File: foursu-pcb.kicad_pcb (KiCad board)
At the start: 2 copper layers, 71.4 x 38.1 mm, 24 parts, among them SW1 SW_Push, U1 ATmega32U4-AU, Y1 16MHz

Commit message: uh yes microcontroller stuff
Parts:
- moved C3 13.9 mm to (37.3, 129.1), turned to 270 degrees
- moved C2 8.76 mm to (46.8, 129.4), turned to 90 degrees
- moved C4 8.72 mm to (32.4, 136.5)
- moved C6 8.33 mm to (34.3, 133.3)
- moved Y1 6.54 mm to (42.1, 129.1), turned to 180 degrees
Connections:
- C2 pad 2: Net-(C2-Pad2) -> GND
- C3 pad 2: Net-(C2-Pad2) -> GND
- U1 pad 27: Net-(U1-Pad27) -> ROW0
- U1 pad 28: Net-(U1-Pad28) -> ROW1
- U1 pad 29: Net-(U1-Pad29) -> COL0
- U1 pad 30: Net-(U1-Pad30) -> COL1
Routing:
- net GND: track 0.00 -> 110.4 mm
- net +5V: track 0.00 -> 91.0 mm, vias 0 -> 5
- net ROW1: track 0.00 -> 58.3 mm
- net COL1: track 0.00 -> 57.5 mm, vias 0 -> 1
- net ROW0: track 0.00 -> 54.5 mm
- net COL0: track 0.00 -> 32.4 mm, vias 0 -> 1
- net Net-(R3-Pad2): track 0.00 -> 29.2 mm, vias 0 -> 2
- net Net-(C3-Pad1): track 0.00 -> 12.7 mm
- net Net-(C2-Pad1): track 3.70 -> 10.6 mm
- net Net-(D2-Pad2): track 0.00 -> 6.82 mm
- net Net-(D4-Pad2): track 0.00 -> 6.62 mm
- net Net-(D1-Pad2): track 0.00 -> 6.62 mm
- net Net-(D3-Pad2): track 0.00 -> 6.62 mm
- net Net-(C4-Pad1): track 0.00 -> 6.32 mm
- net VCC: track 0.00 -> 5.07 mm
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
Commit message: finished first prototype?
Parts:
- removed C1, C5, C6: 0.1uF, Capacitor_SMD:C_0805_2012Metric
- removed C2, C3: 22pF, Capacitor_SMD:C_0805_2012Metric
- removed C4: 1uF, Capacitor_SMD:C_0805_2012Metric
- removed C7: 10uF, Capacitor_SMD:C_0805_2012Metric
- removed F1: Polyfuse, Fuse:Fuse_1206_3216Metric
- removed R1, R2: 22, Resistor_SMD:R_0805_2012Metric
- removed R3, R4: 10k, Resistor_SMD:R_0805_2012Metric
- removed U1: ATmega32U4-AU, Package_QFP:TQFP-44_10x10mm_P0.8mm
- removed USB1: Molex-0548190519, random-keyboard-parts:Molex-0548190589
- removed Y1: 16MHz, Crystal:Crystal_SMD_3225-4Pin_3.2x2.5mm
- added B1: SPARKFUN_PRO_MICRO, Boards:SPARKFUN_PRO_MICRO, F.Cu at (57.5, 137.5)
- added D5: 1N4148, Diode_THT:D_DO-35_SOD27_P7.62mm_Horizontal, B.Cu at (91.6, 161.8)
- D1, D2, D3, D4: value SOD-123 -> 1N4148; footprint Diode_SMD:D_SOD-123 -> Diode_THT:D_DO-35_SOD27_P7.62mm_Horizontal
- MX1, MX2, MX3, MX4: value MX-NoLED -> MX-LED; footprint MX_Alps_Hybrid:MX-1U-NoLED -> MX_Only:MXOnly-1U
- SW1: value SW_Push -> Rotary_Encoder_Switch; footprint random-keyboard-parts:SKQG-1155865 -> Rotary_Encoder:RotaryEncoder_Alps_EC11E-Switch_Vertical_H20mm; moved to F.Cu
- moved SW1 70.2 mm to (94.1, 130.3), turned to 270 degrees
- moved D3 49.9 mm to (107.6, 173.8), turned to 12 degrees
- moved D1 47.4 mm to (48.0, 168.1), turned to 348 degrees
- moved MX4 46.8 mm to (127.8, 157.8), turned to 12 degrees
- moved MX3 43.9 mm to (109.3, 161.8), turned to 12 degrees
- moved D4 42.9 mm to (126.2, 169.9), turned to 12 degrees
- moved MX1 31.9 mm to (55.5, 157.8), turned to 348 degrees
- moved D2 27.4 mm to (66.2, 172.9), turned to 348 degrees
- moved MX2 18.9 mm to (74.0, 161.8), turned to 348 degrees
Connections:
- D2 pad 1: ROW1 -> ROW0
- D4 pad 1: ROW1 -> ROW0
- MX2 pad 1: COL0 -> COL1
- MX3 pad 1: COL1 -> COL2
- MX4 pad 1: COL1 -> COL3
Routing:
- net +5V: track 91.0 -> 0.00 mm, vias 5 -> 0
- net ROW0: track 54.5 -> 133.6 mm
- net GND: track 110.4 -> 46.5 mm
- net COL3: track 0.00 -> 58.6 mm
- net ROW1: track 58.3 -> 0.00 mm
- net COL2: track 0.00 -> 43.6 mm
- net COL1: track 57.5 -> 15.7 mm, vias 1 -> 0
- net ENC0: track 0.00 -> 37.8 mm
- net ENC1: track 0.00 -> 37.7 mm
- net Net-(R3-Pad2): track 29.2 -> 0.00 mm, vias 2 -> 0
- net COL4: track 0.00 -> 22.4 mm
- net Net-(R1-Pad1): track 20.7 -> 0.00 mm
- net COL0: track 32.4 -> 12.6 mm, vias 1 -> 0
- net Net-(R2-Pad1): track 19.0 -> 0.00 mm
- net Net-(C3-Pad1): track 12.7 -> 0.00 mm
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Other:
- board size 71.4 x 38.1 mm -> 103.3 x 61.2 mm

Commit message: files for initial prototype
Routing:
- net (no net): vias 0 -> 3
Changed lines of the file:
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@@
     (thickness 1.6)
     (drawings 67)
-    (tracks 65)
+    (tracks 68)
     (zones 0)
     (modules 11)
@@
   (gr_circle (center 140.484886 170.047964) (end 142.184886 170.047964) (layer Dwgs.User) (width 0.2))
   (gr_line (start 91.64375 183.225) (end 143.284886 172.248337) (layer Dwgs.User) (width 0.2))
+  (via (at 24.60625 227.0125) (size 0.8) (drill 0.4) (layers F.Cu B.Cu) (net 0))
+  (via (at 76.99375 217.4875) (size 0.8) (drill 0.4) (layers F.Cu B.Cu) (net 0))
+  (via (at 169.06875 109.5375) (size 0.8) (drill 0.4) (layers F.Cu B.Cu) (net 0))
   (segment (start 90.239499 128.909499) (end 77.386565 128.909499) (width 0.381) (layer B.Cu) (net 1))
   (segment (start 91.63 130.3) (end 90.239499 128.909499) (width 0.381) (layer B.Cu) (net 1))

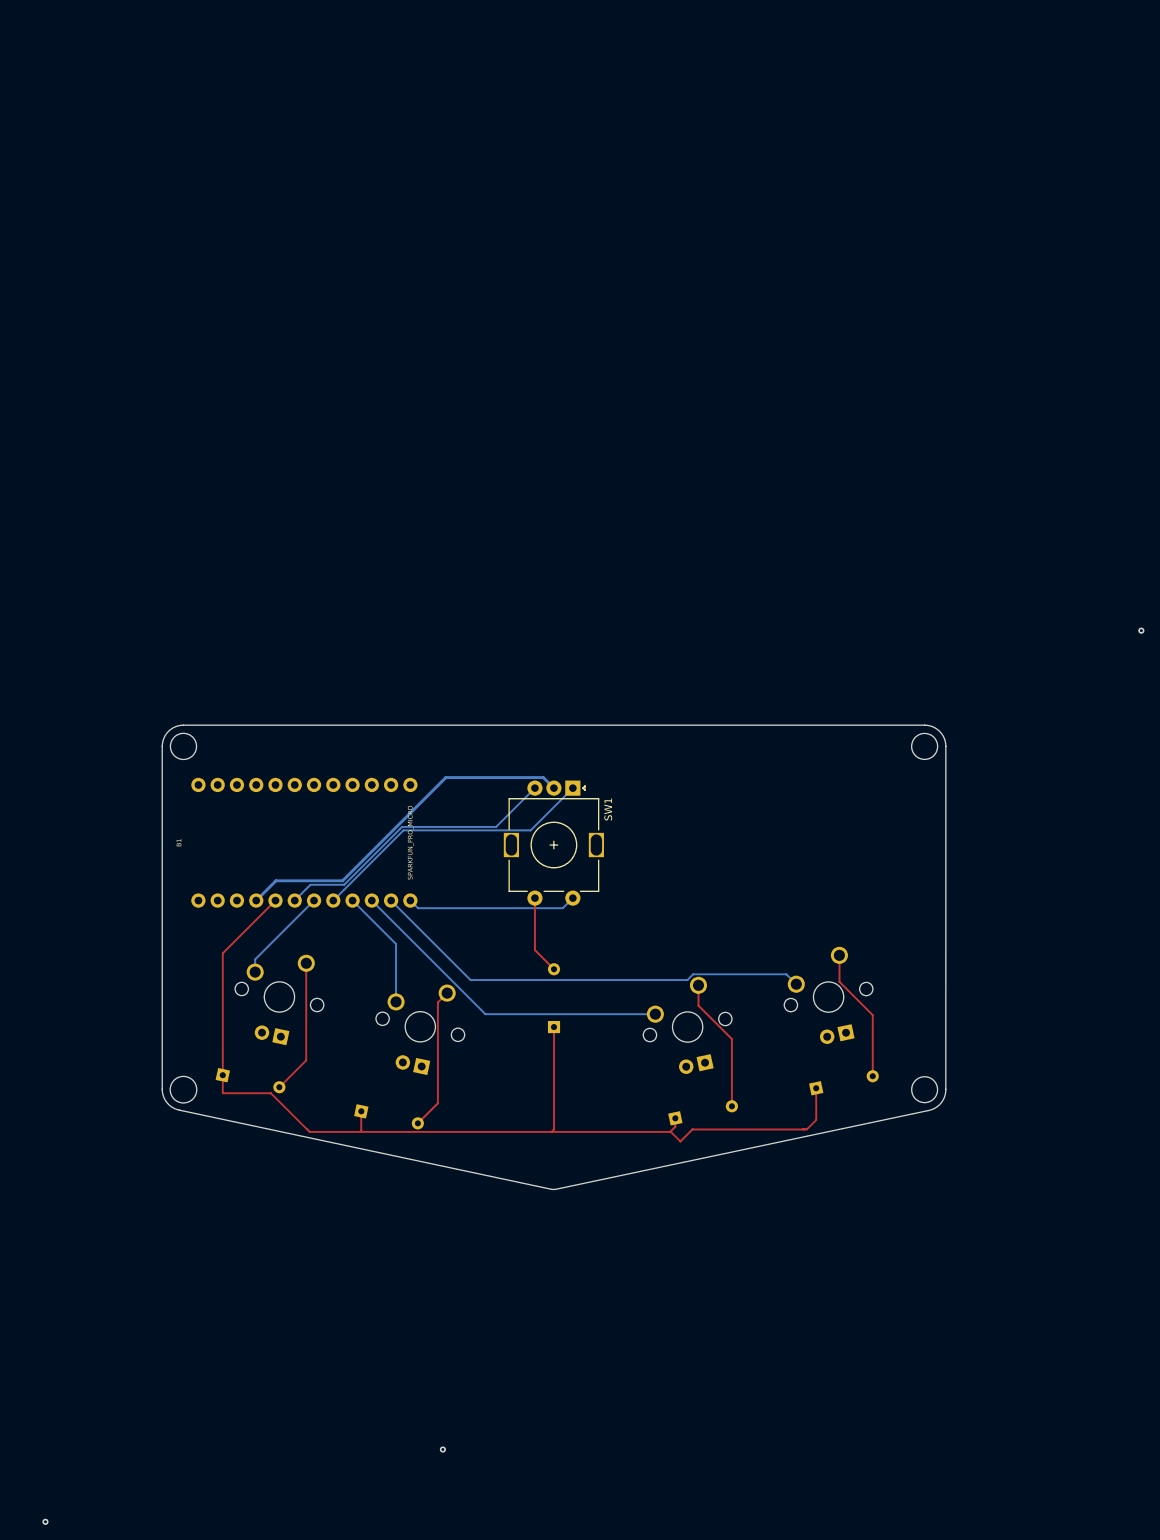
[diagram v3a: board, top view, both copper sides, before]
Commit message: finished pcb routing
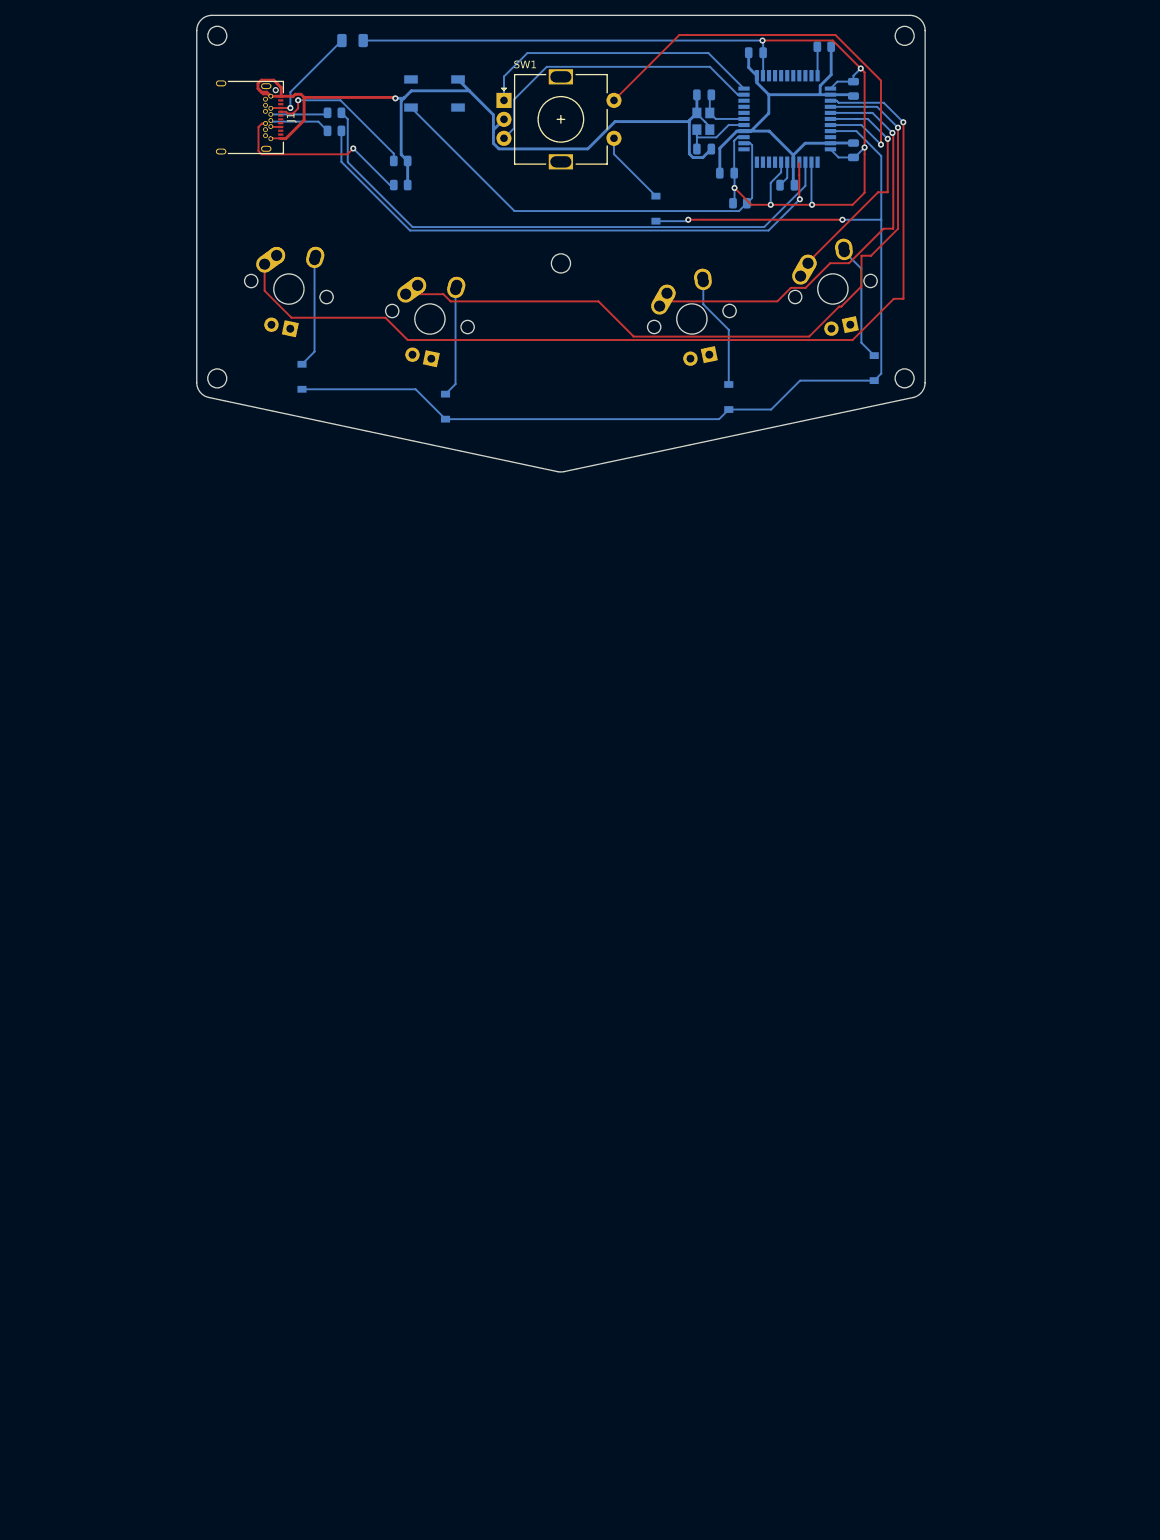
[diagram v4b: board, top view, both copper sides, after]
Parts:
- removed B1: SPARKFUN_PRO_MICRO, Boards:SPARKFUN_PRO_MICRO
- added C1: 0.1uF, Capacitor_SMD:C_0805_2012Metric, B.Cu at (118.3, 33.4)
- added C2: 0.1uF, Capacitor_SMD:C_0805_2012Metric, B.Cu at (114.4, 49.2)
- added C3: 22pF, Capacitor_SMD:C_0805_2012Metric, B.Cu at (111.4, 38.9)
- added C4: 22pF, Capacitor_SMD:C_0805_2012Metric, B.Cu at (111.4, 46.1)
- added C5: 0.1uF, Capacitor_SMD:C_0805_2012Metric, B.Cu at (131.1, 38.1)
- added C6: 10uF, Capacitor_SMD:C_0805_2012Metric, B.Cu at (131.1, 46.2)
- added C7: 1uF, Capacitor_SMD:C_0805_2012Metric, B.Cu at (122.4, 50.8)
- added F1: Polyfuse, Fuse:Fuse_1206_3216Metric, B.Cu at (65.1, 31.8)
- added J1: USB_C_Receptacle_USB2.0, Connector_USB:USB_C_Receptacle_Amphenol_12401548E4-2A, F.Cu at (50.6, 41.9)
- added R1: 22, Resistor_SMD:R_0805_2012Metric, B.Cu at (62.7, 41.3)
- added R2: 22, Resistor_SMD:R_0805_2012Metric, B.Cu at (62.7, 43.7)
- added R3: 10k, Resistor_SMD:R_0805_2012Metric, B.Cu at (116.2, 53.2)
- added R4: 10k, Resistor_SMD:R_0805_2012Metric, B.Cu at (127.3, 32.6)
- added R5: 5.1K, Resistor_SMD:R_0805_2012Metric, B.Cu at (71.4, 47.6)
- added R6: 5.1K, Resistor_SMD:R_0805_2012Metric, B.Cu at (71.4, 50.8)
- added SW2: SW_Push, random-keyboard-parts:SKQG-1155865, B.Cu at (75.9, 38.7)
- added U1: ATmega32U4-AU, Package_QFP:TQFP-44_10x10mm_P0.8mm, B.Cu at (122.4, 42.1)
- added Y1: 16MHz, Crystal:Crystal_SMD_3225-4Pin_3.2x2.5mm, B.Cu at (111.3, 42.4)
- D1, D2, D3, D4, D5: value 1N4148 -> SOD-123; footprint Diode_THT:D_DO-35_SOD27_P7.62mm_Horizontal -> Diode_SMD:D_SOD-123
- MX1, MX2, MX3, MX4: value MX-LED -> MX-NoLED; footprint MX_Only:MXOnly-1U -> MX_Alps_Hybrid:MX-1U
- moved D5 108.7 mm to (105.1, 53.9)
- moved D3 95.3 mm to (114.7, 78.7), turned to 90 degrees
- moved D4 95.2 mm to (133.9, 74.9), turned to 90 degrees
- moved D2 93.6 mm to (77.3, 80.0), turned to 90 degrees
- moved MX4 93.3 mm to (128.4, 64.5)
- moved MX3 93.3 mm to (109.8, 68.5)
- moved MX1 93.3 mm to (56.7, 64.5)
- moved MX2 93.3 mm to (75.3, 68.5)
- moved D1 92.7 mm to (58.4, 76.1), turned to 90 degrees
- moved SW1 91.1 mm to (85.0, 39.6), turned to 0 degrees
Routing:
- net +5V: track 0.00 -> 139.8 mm, vias 0 -> 6
- net GND: track 46.5 -> 171.1 mm, vias 0 -> 1
- net COL0: track 12.6 -> 126.7 mm, vias 0 -> 1
- net COL1: track 15.7 -> 99.1 mm, vias 0 -> 1
- net Net-(R1-Pad1): track 0.00 -> 76.1 mm
- net Net-(R2-Pad1): track 0.00 -> 74.8 mm, vias 0 -> 1
- net Net-(R3-Pad2): track 0.00 -> 59.5 mm
- net COL4: track 22.4 -> 57.4 mm, vias 0 -> 1
- net COL3: track 58.6 -> 32.6 mm, vias 0 -> 1
- net Net-(J1-PadB5): track 0.00 -> 24.8 mm, vias 0 -> 1
- net Net-(J1-PadA5): track 0.00 -> 20.2 mm, vias 0 -> 1
- net VCC: track 0.00 -> 15.6 mm, vias 0 -> 1
- net COL2: track 43.6 -> 57.5 mm, vias 0 -> 1
- net ROW0: track 133.6 -> 147.0 mm, vias 0 -> 2
- net Net-(C4-Pad1): track 0.00 -> 10.4 mm
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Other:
- board size 103.3 x 61.2 mm -> 96 x 60.2 mm

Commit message: yeh
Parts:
- moved C2 0.68 mm to (114.4, 49.9)
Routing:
- added copper zone on B.Cu, net GND
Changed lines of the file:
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@@
     (thickness 1.6)
     (drawings 68)
-    (tracks 300)
+    (tracks 302)
     (zones 0)
     (modules 28)
@@
   )
   (module Capacitor_SMD:C_0805_2012Metric (layer B.Cu)
-    (at 114.44875 49.23 180)
+    (at 114.44875 49.911 180)
     (descr "Capacitor SMD 0805 (2012 Metric), square (rectangular) end terminal, IPC_7351 nominal, (Body size source: IPC-SM-782 page 76, https://www.pcb-3d.com/wordpress/wp-content/uploads/ipc-sm-782a_amendment_1_and_2.pdf, https://docs.google.com/spreadsheets/d/1BsfQQcO9C6DZCsRaXUlFlo91Tg2WpOkGARC1WS5S8t0/edit?usp=sharing), generated with kicad-footprint-generator")
     (tags capacitor)
@@
   (gr_arc (start 92.54 86.63) (end 92.120001 88.579999) (angle -24.87027869) (layer Edge.Cuts) (width 0.05))
   (gr_arc (start 138.56 76.85) (end 138.969999 78.809999) (angle -77.8971087) (layer Edge.Cuts) (width 0.05))
-  (segment (start 134.747 45.466) (end 132.16725 42.88625) (width 0.254) (layer B.Cu) (net 1))
-  (segment (start 132.16725 42.88625) (end 128.08625 42.88625) (width 0.254) (layer B.Cu) (net 1))
   (segment (start 99.55 39.64) (end 108.167001 31.022999) (width 0.254) (layer F.Cu) (net 1))
   (segment (start 108.167001 31.022999) (end 128.745961 31.022999) (width 0.254) (layer F.Cu) (net 1))
@@
   (segment (start 134.747 37.024038) (end 134.747 45.466) (width 0.254) (layer F.Cu) (net 1))
   (via (at 134.747 45.466) (size 0.8) (drill 0.4) (layers F.Cu B.Cu) (net 1))
+  (segment (start 132.16725 42.88625) (end 128.08625 42.88625) (width 0.254) (layer B.Cu) (net 1))
+  (segment (start 134.747 45.466) (end 132.16725 42.88625) (width 0.254) (layer B.Cu) (net 1))
   (segment (start 134.366 51.748962) (end 135.636 51.748962) (width 0.254) (layer F.Cu) (net 2))
   (segment (start 131.74825 42.08625) (end 131.36725 42.08625) (width 0.254) (layer B.Cu) (net 2))
@@
   (segment (start 99.55 44.64) (end 99.55 46.73) (width 0.254) (layer B.Cu) (net 14))
   (segment (start 99.55 46.73) (end 105.08 52.26) (width 0.254) (layer B.Cu) (net 14))
-  (segment (start 117.663452 53.401452) (end 120.207548 53.401452) (width 0.254) (layer F.Cu) (net 15))
   (segment (start 121.58625 49.126482) (end 120.207548 50.505184) (width 0.254) (layer B.Cu) (net 15))
   (segment (start 120.207548 50.505184) (end 120.207548 53.401452) (width 0.254) (layer B.Cu) (net 15))
@@
   (via (at 125.664452 53.401452) (size 0.8) (drill 0.4) (layers F.Cu B.Cu) (net 15))
   (segment (start 125.664452 53.401452) (end 131.002548 53.401452) (width 0.254) (layer F.Cu) (net 15))
-  (segment (start 115.443 51.181) (end 117.663452 53.401452) (width 0.254) (layer F.Cu) (net 15))
   (segment (start 131.002548 53.401452) (end 132.588 51.816) (width 0.254) (layer F.Cu) (net 15))
   (segment (start 132.588 51.816) (end 132.588 46.736) (width 0.254) (layer F.Cu) (net 15))
@@
   (segment (start 131.27375 47.16125) (end 132.588 45.847) (width 0.254) (layer B.Cu) (net 15))
   (via (at 132.588 45.847) (size 0.8) (drill 0.4) (layers F.Cu B.Cu) (net 15))
-  (segment (start 115.443 51.181) (end 115.443 52.99825) (width 0.254) (layer B.Cu) (net 15))
   (segment (start 115.443 52.99825) (end 115.2425 53.19875) (width 0.254) (layer B.Cu) (net 15))
   (segment (start 115.443 51.181) (end 115.443 49.27425) (width 0.254) (layer B.Cu) (net 15))
   (segment (start 115.443 49.27425) (end 115.39875 49.23) (width 0.254) (layer B.Cu) (net 15))
-  (via (at 115.443 51.181) (size 0.8) (drill 0.4) (layers F.Cu B.Cu) (net 15))
   (segment (start 119.126 31.75) (end 128.397 31.75) (width 0.254) (layer F.Cu) (net 15))
   (segment (start 66.4875 31.75) (end 119.126 31.75) (width 0.254) (layer B.Cu) (net 15))
@@
   (segment (start 131.1175 47.16125) (end 129.16125 47.16125) (width 0.254) (layer B.Cu) (net 15))
   (segment (start 129.16125 47.16125) (end 128.08625 46.08625) (width 0.254) (layer B.Cu) (net 15))
+  (via (at 116.586 51.689) (size 0.8) (drill 0.4) (layers F.Cu B.Cu) (net 15))
+  (segment (start 118.298452 53.401452) (end 116.586 51.689) (width 0.254) (layer F.Cu) (net 15))
+  (segment (start 120.207548 53.401452) (end 118.298452 53.401452) (width 0.254) (layer F.Cu) (net 15))
+  (segment (start 116.586 51.689) (end 115.443 51.689) (width 0.254) (layer B.Cu) (net 15))
+  (segment (start 115.443 51.689) (end 115.443 52.99825) (width 0.254) (layer B.Cu) (net 15))
+  (segment (start 115.443 51.181) (end 115.443 51.689) (width 0.254) (layer B.Cu) (net 15))
   (segment (start 112.18 41.2925) (end 112.18 39.11125) (width 0.254) (layer B.Cu) (net 16))
   (segment (start 112.18 39.11125) (end 112.38 38.91125) (width 0.254) (layer B.Cu) (net 16))
@@
   (segment (start 126.38625 36.38625) (end 126.38625 32.5925) (width 0.254) (layer B.Cu) (net 32))
   (segment (start 126.38625 32.5925) (end 126.355 32.56125) (width 0.254) (layer B.Cu) (net 32))
+  (zone (net 9) (net_name GND) (layer B.Cu) (hatch edge 0.508)
+    (connect_pads (clearance 0.508))
+    (min_thickness 0.254)
+    (fill yes (arc_segments 32) (thermal_gap 0.508) (thermal_bridge_width 0.508))
+    (polygon
+      (pts
+        (xy 140.589 53.213) (xy 44.577 53.34) (xy 44.577 28.448) (xy 140.589 28.448)
+      )
+    )
+  )
 )

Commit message: some commit idk
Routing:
- net COL3: track 32.6 -> 31.9 mm
- net COL2: track 57.5 -> 56.9 mm
- net ROW0: track 147.0 -> 147.6 mm
